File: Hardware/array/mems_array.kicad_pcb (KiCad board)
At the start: 4 copper layers, 350 x 190 mm, 61 parts, among them U101 74AHC244, U102 743245, U103 741G04, U104 BEAGLEBONEBLACK, U201 SN74CTBLV3251, U301 SN74CTBLV3251, U401 SN74CTBLV3251, U501 SN74CTBLV3251, U601 SN74CTBLV3251

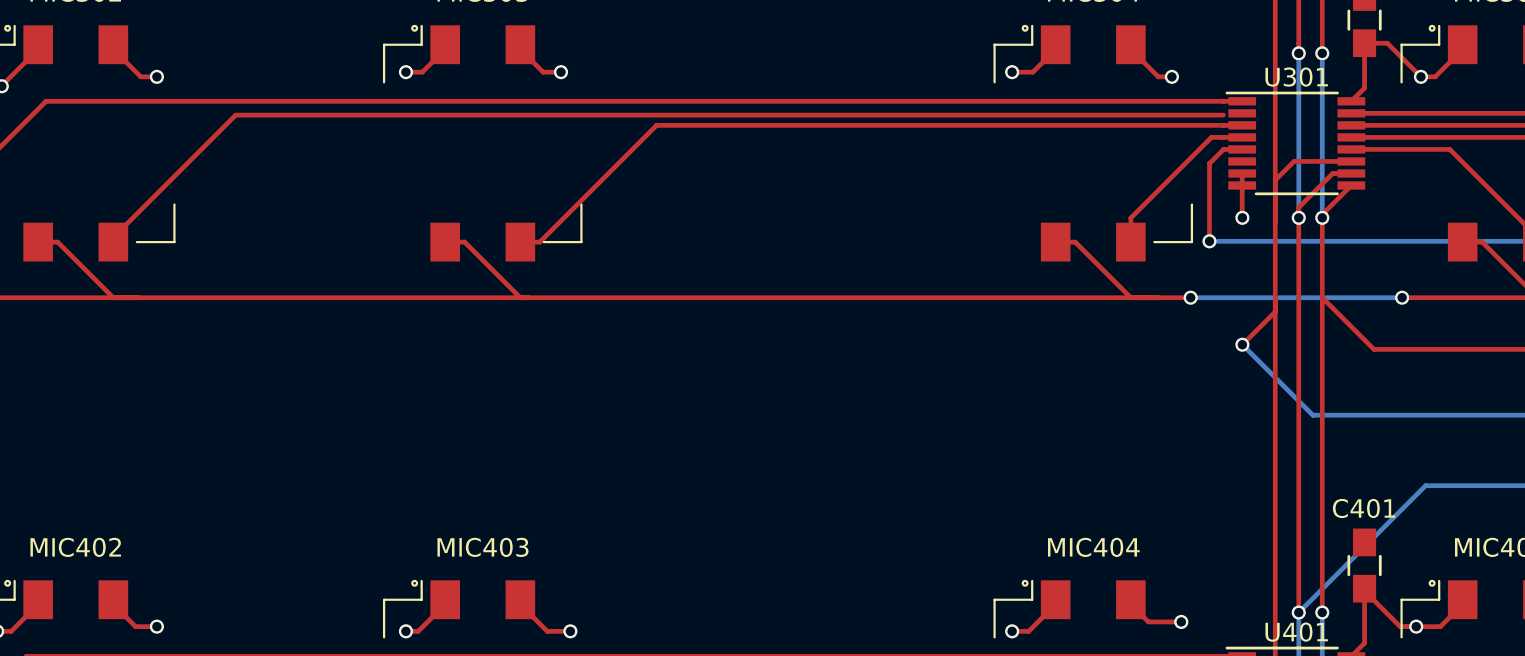
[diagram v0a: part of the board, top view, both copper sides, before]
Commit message: Fix unconnected pins.
Signed-off-by: Chamon <luizchamon@gmail.com>
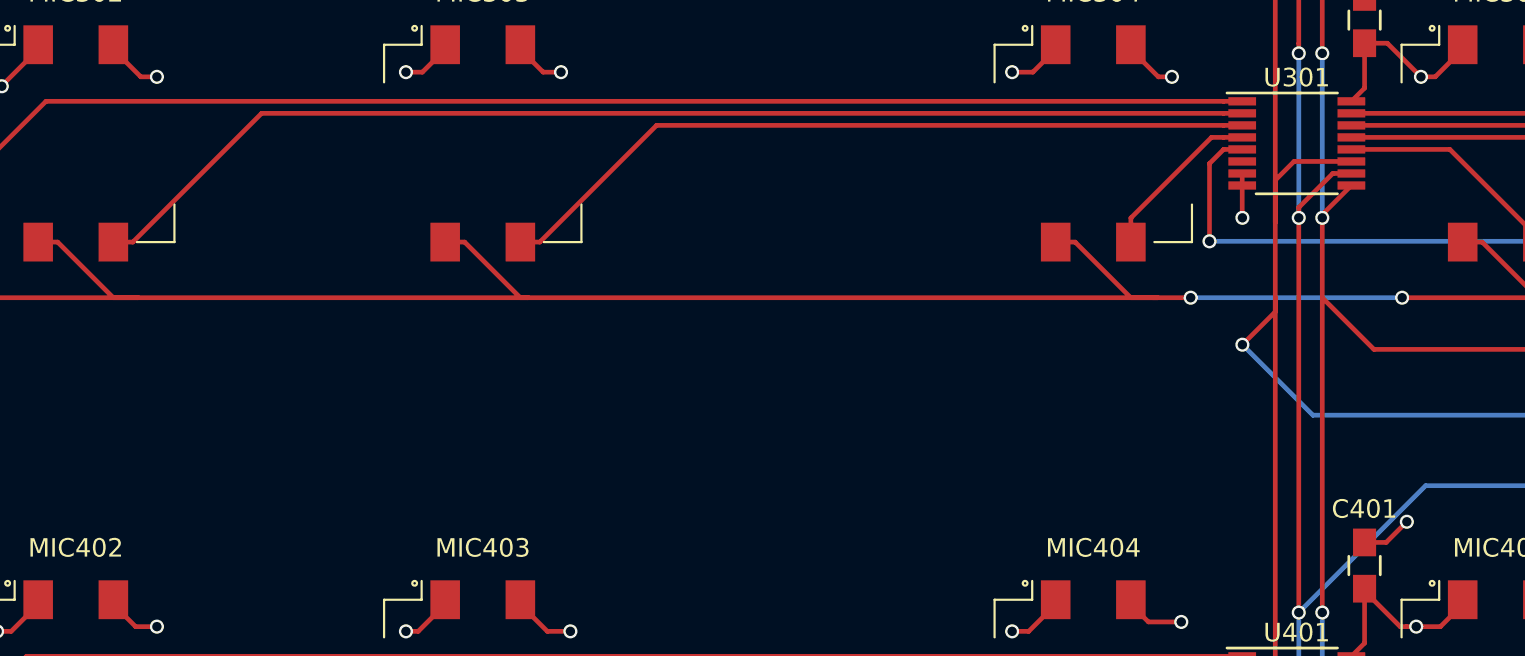
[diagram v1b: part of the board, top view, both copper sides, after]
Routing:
- net DGND: track 183.1 -> 185.9 mm, vias 54 -> 55
- net Net-(MIC302-Pad3): track 63.0 -> 64.2 mm
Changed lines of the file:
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@@
   (general
     (links 245)
-    (no_connects 2)
-    (area -10.075001 -5.075001 340.075001 185.075001)
+    (no_connects 0)
+    (area 29.924999 29.924999 380.075001 220.075001)
     (thickness 1.6)
     (drawings 8)
-    (tracks 983)
+    (tracks 988)
     (zones 0)
     (modules 61)
@@
     (1 Ground_plane power)
     (2 Power_plane power)
-    (31 B.Cu signal)
+    (31 B.Cu signal hide)
     (32 B.Adhes user)
     (33 F.Adhes user)
@@
   (segment (start 62.968 56.228) (end 62.098 57.098) (width 0.254) (layer F.Cu) (net 1))
   (via (at 62.098 57.098) (size 0.762) (drill 0.508) (layers F.Cu B.Cu) (net 1))
+  (segment (start 145.664 101.568) (end 146.831962 101.568) (width 0.254) (layer F.Cu) (net 2))
+  (segment (start 146.831962 101.568) (end 147.948981 100.450981) (width 0.254) (layer F.Cu) (net 2))
+  (via (at 147.948981 100.450981) (size 0.762) (drill 0.508) (layers F.Cu B.Cu) (net 2))
   (segment (start 287 165.2512) (end 297.3562 165.2512) (width 0.508) (layer F.Cu) (net 2))
   (segment (start 297.3562 165.2512) (end 297.6 165.495) (width 0.508) (layer F.Cu) (net 2))
@@
   (segment (start 74.391 77.725) (end 138.046 77.725) (width 0.254) (layer F.Cu) (net 13))
   (segment (start 138.046 77.725) (end 139.05 77.725) (width 0.254) (layer F.Cu) (net 13))
+  (segment (start 78.032 85.334) (end 79.086 85.334) (width 0.254) (layer F.Cu) (net 14))
+  (segment (start 79.086 85.334) (end 86.045 78.375) (width 0.254) (layer F.Cu) (net 14))
+  (segment (start 86.045 78.375) (end 138.046 78.375) (width 0.254) (layer F.Cu) (net 14))
+  (segment (start 138.046 78.375) (end 139.05 78.375) (width 0.254) (layer F.Cu) (net 14))
   (segment (start 78.032 85.334) (end 78.032 85.084) (width 0.254) (layer F.Cu) (net 14))
-  (segment (start 78.032 85.084) (end 84.646201 78.469799) (width 0.254) (layer F.Cu) (net 14))
-  (segment (start 84.646201 78.469799) (end 138.035839 78.469799) (width 0.254) (layer F.Cu) (net 14))
   (segment (start 100.032 85.334) (end 101.086 85.334) (width 0.254) (layer F.Cu) (net 15))
   (segment (start 101.086 85.334) (end 107.395 79.025) (width 0.254) (layer F.Cu) (net 15))
